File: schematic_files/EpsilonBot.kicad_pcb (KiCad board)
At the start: 2 copper layers, 241.5 x 110.5 mm, 15 parts, among them J1 USB C PD Modulle, J2 LIDAR, J3 MOTOR_L, J4 MOTOR_R, SW1 SW_SPDT, U1 RPLIDAR C1, U1 Radxa_ROCK5B, U2 Buck Converter

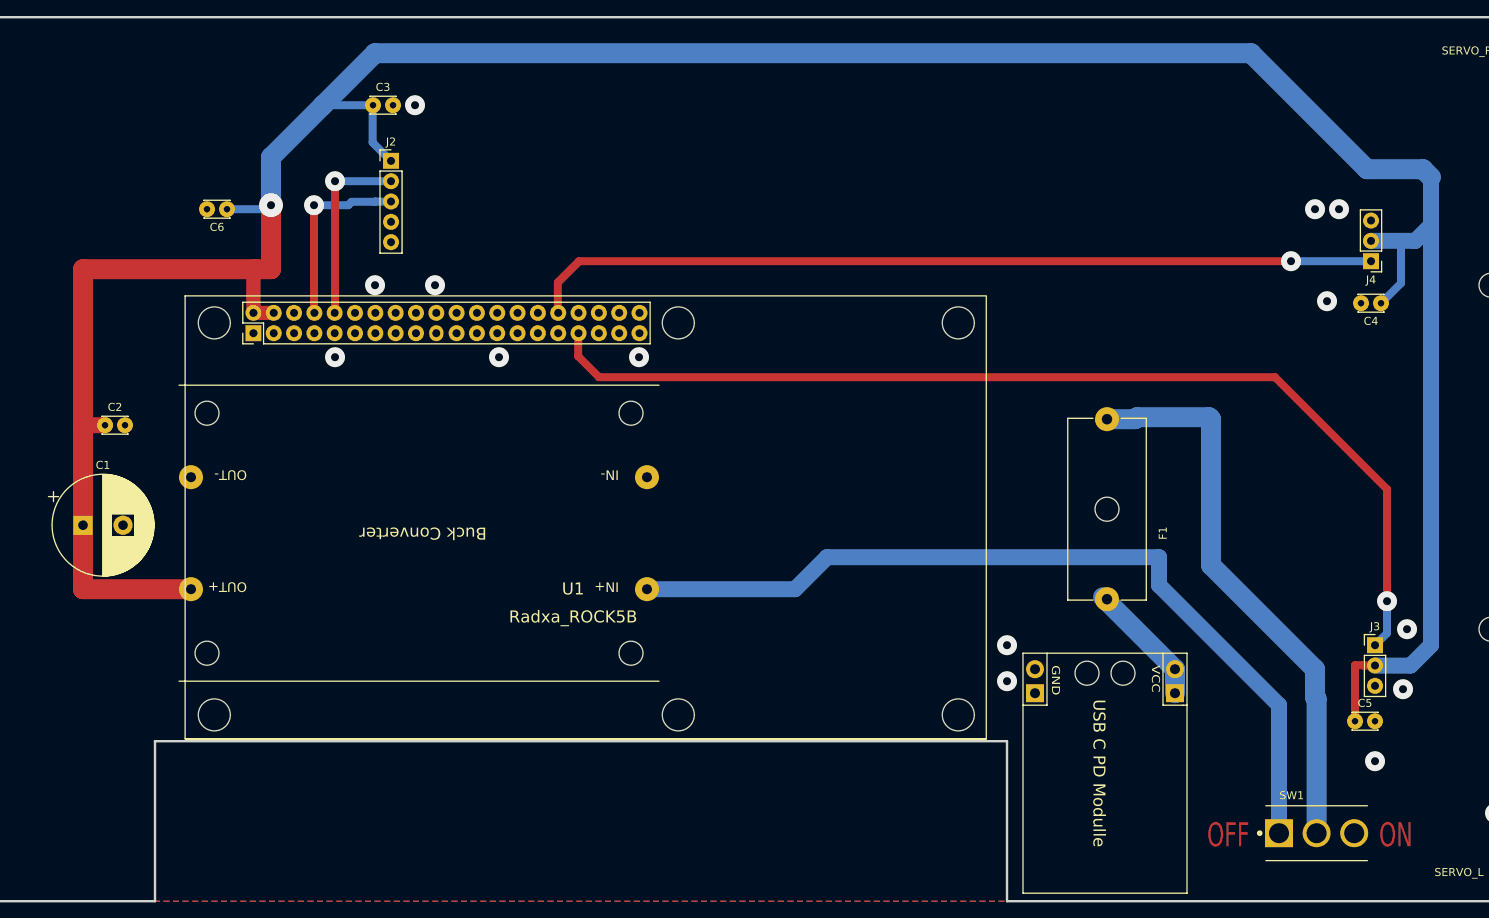
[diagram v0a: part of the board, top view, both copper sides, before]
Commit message: Updated PCB layout for the RPI
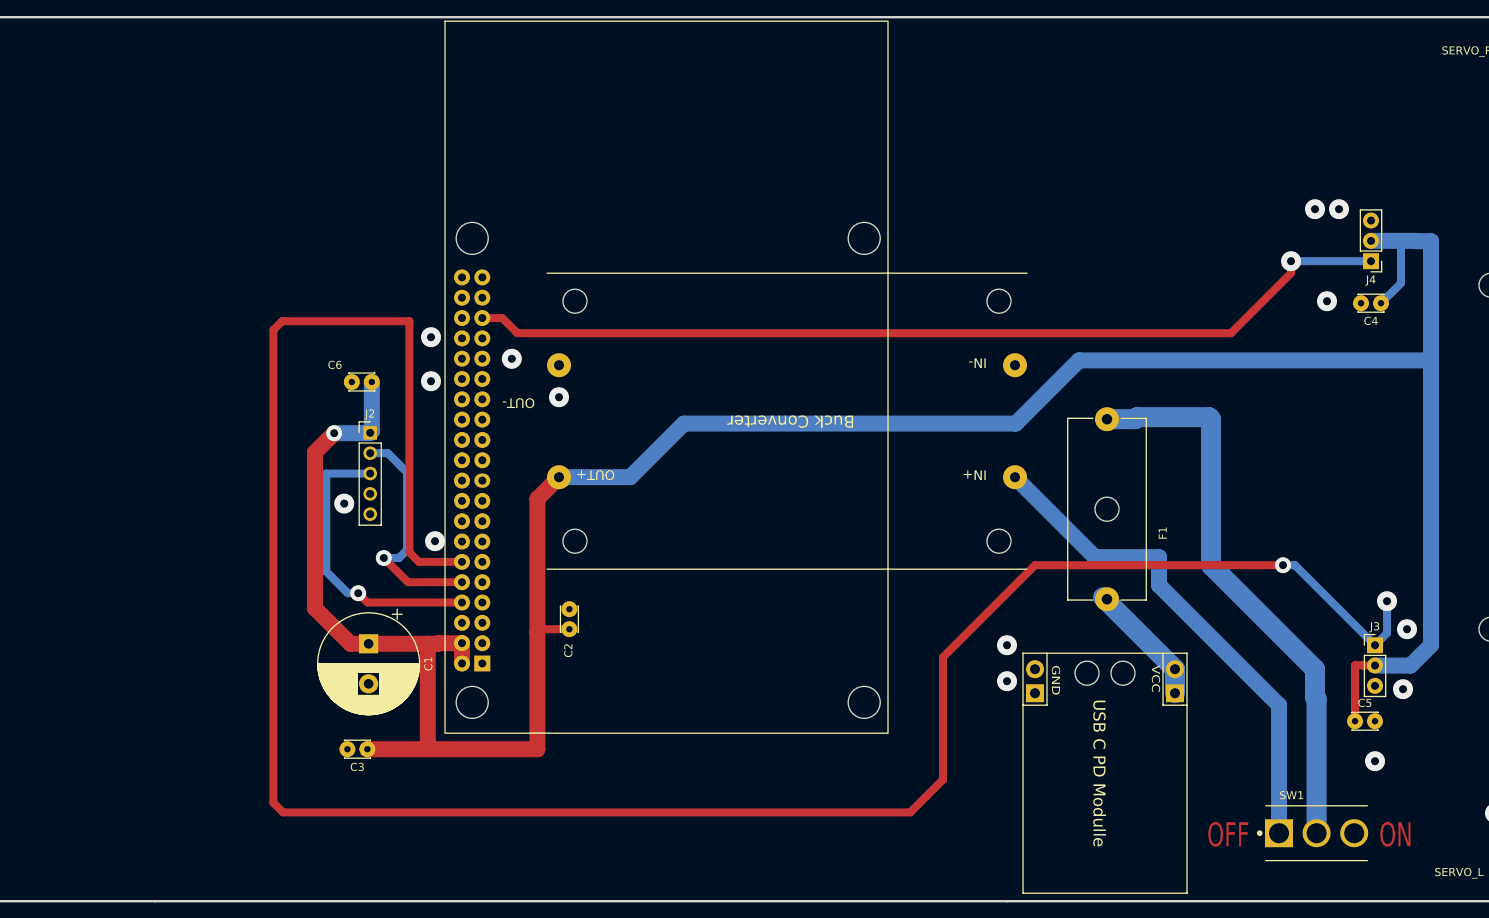
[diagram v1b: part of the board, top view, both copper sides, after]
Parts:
- J2: value LIDAR -> Conn_01x05; footprint deltabot:PinHeader_1x05_P2.54mm_Vertical -> Connector_PinHeader_2.54mm:PinHeader_1x05_P2.54mm_Vertical
- U1: value Radxa_ROCK5B -> RPI5; footprint deltabot:ROCK_5B -> epsilon:RPI5; moved to B.Cu
- moved C3 80.5 mm to (76.0, 127.5), turned to 180 degrees
- moved C2 63.4 mm to (101.3, 112.5), turned to 90 degrees
- moved U2 48.1 mm to (129.0, 86.5)
- moved C1 38.7 mm to (76.2, 114.3), turned to -90 degrees
- moved J2 34.1 mm to (76.4, 88.0)
- moved C6 28.2 mm to (76.6, 81.6)
- moved U1 22.1 mm to (123.9, 108.5), turned to -90 degrees
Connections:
- U1 pad 12: unconnected-(U1-GPIO4_A3-Pad12) -> PWM_L
- U1 pad 18: MOTO_CTRL -> unconnected-(U1-GPIO24-Pad18)
- U1 pad 32: PWM_R -> unconnected-(U1-GPIO12-Pad32)
- U1 pad 33: PWM_L -> unconnected-(U1-GPIO13-Pad33)
- U1 pad 35: unconnected-(U1-GPIO4_A5-Pad35) -> PWM_R
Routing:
- net PWM_L: track 130.8 -> 282.8 mm, vias 1 -> 2
- net +9V: track 106.4 -> 62.9 mm
- net +5V: track 372.2 -> 330.0 mm
- net LIDAR_RX: track 23.4 -> 36.3 mm
- net PWM_R: track 106.7 -> 116.5 mm
- net LIDAR_TX: track 23.7 -> 30.0 mm
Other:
- outline, holes or cut-outs redrawn

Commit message: Added missing files
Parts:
- added D1: LED, LED_THT:LED_D5.0mm_Clear, F.Cu at (188.2, 91.0)
- added R1: 330R, Resistor_THT:R_Axial_DIN0207_L6.3mm_D2.5mm_P10.16mm_Horizontal, F.Cu at (197.0, 80.9)
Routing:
- net +5V: track 330.0 -> 339.6 mm
- net Net-(D1-A): track 0.00 -> 6.27 mm
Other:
- outline, holes or cut-outs redrawn
- board text added: "Epsilon-Bot"
- board text removed: "Delta-Bot"
